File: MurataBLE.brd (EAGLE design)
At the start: 50 x 50 mm, 33 parts, among them IC1 IC_LDO_XX1117, IC3 74LVC1G04DCK, Q2 12MHz, SW1 SW_TACTSW_2PP8073, SW2 SW_TACTSW_2PP8073, SW3 SW_TACTSW_2PP8073, U1 IC_BLE_LBCA2HNZYZ-711, X1 TSW-112-02-S-S

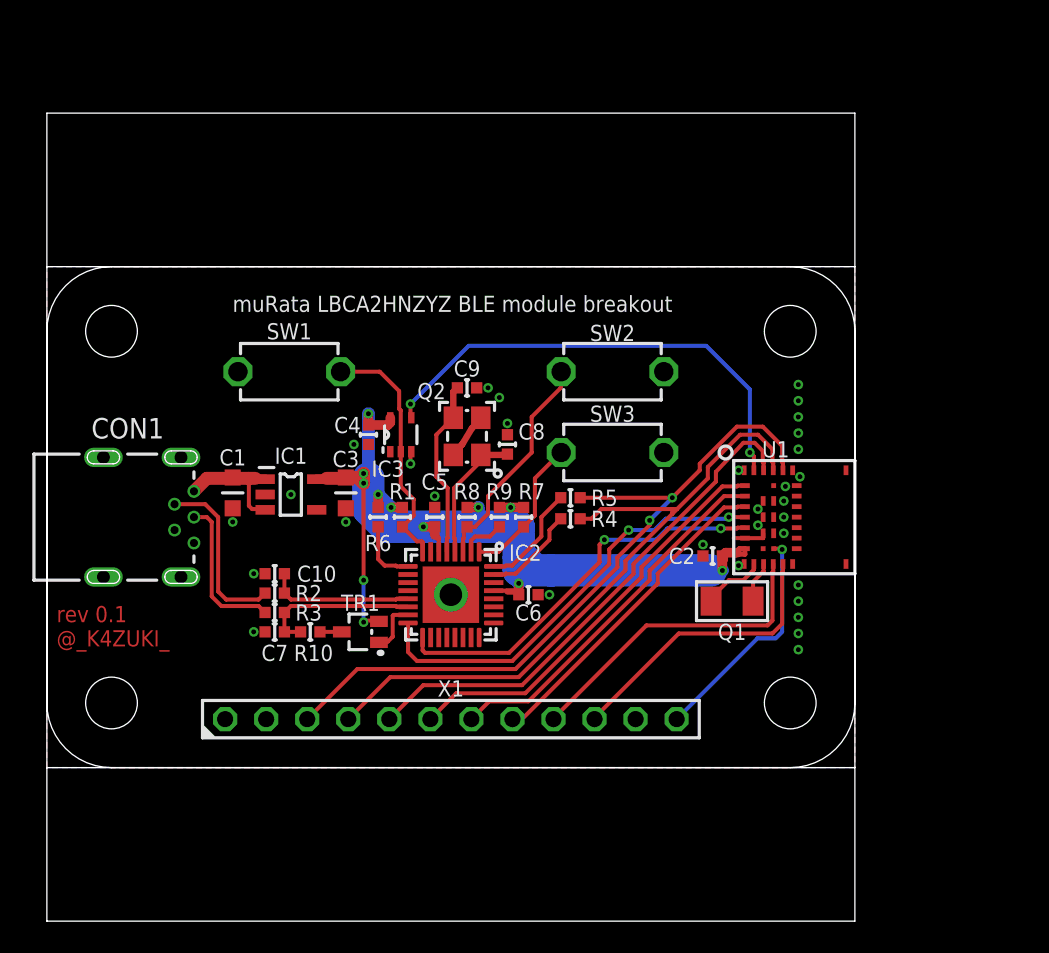
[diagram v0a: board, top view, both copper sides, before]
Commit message: [ BRD ] removed panel frame
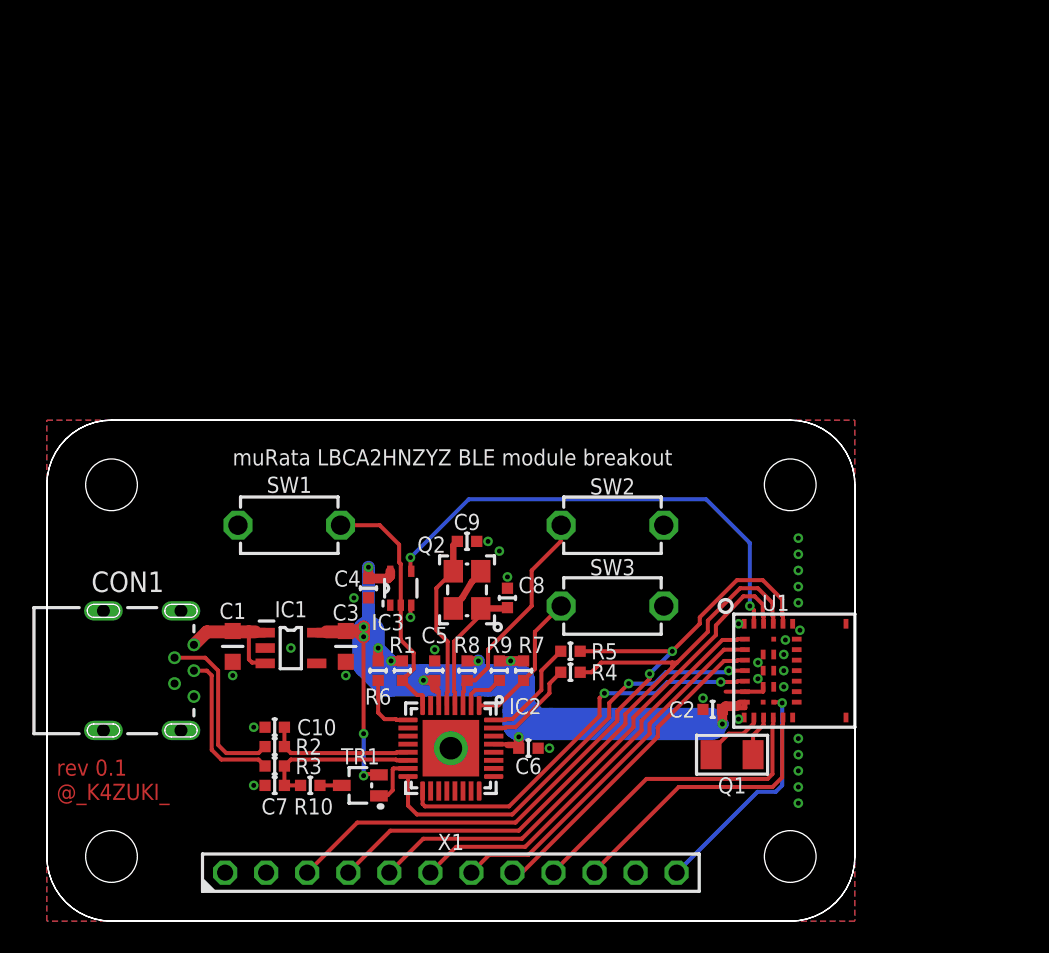
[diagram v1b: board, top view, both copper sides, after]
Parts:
- moved C2 9.50 mm to (41.2, 13.1)
- moved R3 9.50 mm to (14.1, 9.60)
- moved C1 9.50 mm to (11.5, 17.0)
- moved C10 9.50 mm to (14.1, 12.0)
- moved C3 9.50 mm to (18.5, 17.0)
- moved C4 9.50 mm to (19.9, 20.6)
- moved C5 9.50 mm to (24.0, 15.5)
- moved C6 9.50 mm to (29.8, 10.7)
- moved C8 9.50 mm to (28.5, 20.0)
- moved C9 9.50 mm to (26.0, 23.5)
- moved CON1 9.50 mm to (9.10, 15.5)
- moved IC1 9.50 mm to (15.1, 16.9)
- moved IC2 9.50 mm to (25.0, 10.7)
- moved IC3 9.50 mm to (21.9, 20.6)
- moved PCB1 9.50 mm to (25.0, 15.5)
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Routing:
- net GND: track 5.85 -> 6.35 mm
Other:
- board size 50 x 50 mm -> 50 x 31 mm

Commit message: update silk
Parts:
- moved IC3 0.10 mm to (22.0, 20.6)
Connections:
- net 3.3V: now also C3.1; no longer C3.P$1
- net GND: now also C1.2, C3.2; no longer C1.P$2, C3.P$2
- net VUSB: now also C1.1; no longer C1.P$1
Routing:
- net 3.3V: track 72.9 -> 72.1 mm
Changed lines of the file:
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@@
 <wire x1="19" y1="15.5" x2="19" y2="16.6" width="0.15" layer="41"/>
 <wire x1="19" y1="16.6" x2="19" y2="17.3" width="0.15" layer="41"/>
-<wire x1="22.3" y1="19.2" x2="22.3" y2="19.9" width="0.15" layer="41"/>
-<wire x1="22.8" y1="19.2" x2="22.8" y2="19.9" width="0.15" layer="41"/>
-<wire x1="22.8" y1="19.9" x2="22.3" y2="19.9" width="0.15" layer="41"/>
+<wire x1="22.4" y1="19.3" x2="22.4" y2="19.9" width="0.15" layer="41"/>
+<wire x1="22.9" y1="19.3" x2="22.9" y2="19.9" width="0.15" layer="41"/>
+<wire x1="22.9" y1="19.9" x2="22.4" y2="19.9" width="0.15" layer="41"/>
 <wire x1="20.3" y1="19.6" x2="20.3" y2="20.4" width="0.15" layer="41"/>
 <wire x1="20.3" y1="20.4" x2="19.5" y2="20.4" width="0.15" layer="41"/>
@@
 <attribute name="VALUE" x="13.5" y="7.7" size="1" layer="27" font="vector" ratio="20"/>
 </element>
-<element name="IC3" library="74xx-little-us_local" package="SC70-5" value="74LVC1G04DCK" x="21.9" y="20.6" smashed="yes">
-<attribute name="NAME" x="21.1" y="18.5" size="1" layer="25" font="vector" ratio="20" align="center"/>
-<attribute name="VALUE" x="19.4" y="18.1" size="1" layer="27" font="vector" ratio="20"/>
+<element name="IC3" library="74xx-little-us_local" package="SC70-5" value="74LVC1G04DCK" x="22" y="20.6" smashed="yes">
+<attribute name="NAME" x="21" y="23" size="1" layer="25" font="vector" ratio="20" align="center"/>
+<attribute name="VALUE" x="19.5" y="18.1" size="1" layer="27" font="vector" ratio="20"/>
 </element>
 <element name="SW2" library="mylib" package="SW_TACTSW_P8073" value="SW_TACTSW_2PP8073" x="35" y="24.5" smashed="yes" rot="R180">
@@
 <contactref element="IC2" pad="EXP"/>
 <contactref element="CON1" pad="GND"/>
-<contactref element="C3" pad="P$2"/>
-<contactref element="C1" pad="P$2"/>
+<contactref element="C3" pad="2"/>
+<contactref element="C1" pad="2"/>
 <contactref element="IC3" pad="3"/>
 <contactref element="IC3" pad="3"/>
@@
 <via x="18.5" y="15.2" extent="1-16" drill="0.3" diameter="0.45"/>
 <via x="19" y="20" extent="1-16" drill="0.3" diameter="0.45"/>
-<via x="22.5" y="18.8" extent="1-16" drill="0.3" diameter="0.45"/>
+<via x="22.6" y="18.8" extent="1-16" drill="0.3" diameter="0.45"/>
 <via x="28" y="22.9" extent="1-16" drill="0.3" diameter="0.45"/>
 <via x="27.3" y="23.5" extent="1-16" drill="0.3" diameter="0.45"/>
@@
 <wire x1="43.2" y1="14.2" x2="44.325" y2="14.2" width="0.25" layer="1"/>
 <wire x1="44.325" y1="14.2" x2="44.325" y2="14.5" width="0.25" layer="1"/>
-<wire x1="22.55" y1="19.55" x2="22.5" y2="19.55" width="0.25" layer="1"/>
-<wire x1="22.5" y1="19.55" x2="22.5" y2="18.8" width="0.25" layer="1"/>
+<wire x1="22.65" y1="19.65" x2="22.6" y2="19.65" width="0.25" layer="1"/>
+<wire x1="22.6" y1="19.65" x2="22.6" y2="18.8" width="0.25" layer="1"/>
 <contactref element="X1" pad="11"/>
 <contactref element="C10" pad="2"/>
@@
 <contactref element="U1" pad="7"/>
 <contactref element="C2" pad="1"/>
-<contactref element="C3" pad="P$1"/>
+<contactref element="C3" pad="1"/>
 <contactref element="IC2" pad="6"/>
 <contactref element="IC2" pad="29"/>
@@
 <via x="23.3" y="14.9" extent="1-16" drill="0.3"/>
 <via x="26.7" y="16.1" extent="1-16" drill="0.3"/>
-<via x="19.6" y="18.2" extent="1-16" drill="0.3"/>
-<via x="19.6" y="17.6" extent="1-16" drill="0.3"/>
-<wire x1="18.5" y1="17.9525" x2="18.4525" y2="17.9525" width="0.8" layer="1"/>
-<wire x1="18.4525" y1="17.9525" x2="18.4" y2="17.9" width="0.8" layer="1"/>
+<via x="19.9" y="18.2" extent="1-16" drill="0.3"/>
+<via x="19.9" y="17.6" extent="1-16" drill="0.3"/>
 <wire x1="16.7" y1="17.85" x2="17.25" y2="17.85" width="0.6" layer="1"/>
 <wire x1="17.25" y1="17.85" x2="17.3" y2="17.9" width="0.6" layer="1"/>
-<wire x1="18.4" y1="17.9" x2="17.3" y2="17.9" width="0.8" layer="1"/>
-<wire x1="19.6" y1="18.2" x2="19.6" y2="17.6" width="0.8" layer="16"/>
-<wire x1="19.6" y1="18.2" x2="19.3" y2="17.9" width="0.8" layer="1"/>
-<wire x1="19.3" y1="17.9" x2="19.6" y2="17.6" width="0.8" layer="1"/>
-<wire x1="19.6" y1="17.6" x2="19.6" y2="18.2" width="0.8" layer="1"/>
-<wire x1="19.6" y1="18.2" x2="19.9" y2="17.9" width="0.8" layer="16"/>
-<wire x1="19.9" y1="17.9" x2="19.6" y2="17.6" width="0.8" layer="16"/>
-<wire x1="18.5" y1="17.9525" x2="19.2475" y2="17.9525" width="0.8" layer="1"/>
-<wire x1="19.2475" y1="17.9525" x2="19.6" y2="17.6" width="0.8" layer="1"/>
+<wire x1="19.9" y1="18.2" x2="19.6" y2="17.9" width="0.8" layer="1"/>
+<wire x1="19.6" y1="17.9" x2="19.9" y2="17.6" width="0.8" layer="1"/>
+<wire x1="19.9" y1="17.6" x2="19.9" y2="18.2" width="0.8" layer="1"/>
 <wire x1="29.5" y1="16.1" x2="28.7" y2="16.1" width="0.6" layer="1"/>
 <wire x1="28.7" y1="16.1" x2="28" y2="16.1" width="0.6" layer="1"/>
 <wire x1="24" y1="14.9" x2="23.3" y2="14.9" width="0.6" layer="1"/>
 <wire x1="22" y1="16.1" x2="21.3" y2="16.1" width="0.6" layer="1"/>
-<wire x1="20.5" y1="16.9" x2="19.9" y2="17.9" width="0.8" layer="16"/>
 <wire x1="21.3" y1="16.1" x2="21.3" y2="14.9" width="0.8" layer="16"/>
-<wire x1="19.9" y1="17.9" x2="19.9" y2="16" width="2" layer="16"/>
+<wire x1="19.9" y1="17.9" x2="19.9" y2="17.6" width="2" layer="16"/>
+<wire x1="19.9" y1="17.6" x2="19.9" y2="16" width="2" layer="16"/>
 <wire x1="19.9" y1="16" x2="21" y2="14.9" width="2" layer="16"/>
 <wire x1="21" y1="14.9" x2="21.3" y2="14.9" width="2" layer="16"/>
-<wire x1="21.3" y1="14.9" x2="23.3" y2="14.9" width="2" layer="16"/>
+<wire x1="21.3" y1="14.9" x2="22.5" y2="14.9" width="2" layer="16"/>
+<wire x1="22.5" y1="14.9" x2="23.3" y2="14.9" width="2" layer="16"/>
 <wire x1="23.3" y1="14.9" x2="26.7" y2="14.9" width="2" layer="16"/>
 <wire x1="26.7" y1="16.1" x2="26.7" y2="14.9" width="0.8" layer="16"/>
 <via x="19.9" y="21.9" extent="1-16" drill="0.3"/>
 <wire x1="19.9" y1="21.9" x2="19.9" y2="21.2" width="0.6" layer="1"/>
-<wire x1="19.9" y1="21.2" x2="21.1" y2="21.2" width="0.6" layer="1"/>
-<wire x1="21.25" y1="21.65" x2="21.25" y2="21.35" width="0.6" layer="1"/>
-<wire x1="21.25" y1="21.35" x2="21.1" y2="21.2" width="0.6" layer="1"/>
+<wire x1="19.9" y1="21.2" x2="21.2" y2="21.2" width="0.6" layer="1"/>
+<wire x1="21.35" y1="21.55" x2="21.35" y2="21.35" width="0.6" layer="1"/>
+<wire x1="21.35" y1="21.35" x2="21.2" y2="21.2" width="0.6" layer="1"/>
 <wire x1="20.5" y1="16.9" x2="21.3" y2="16.1" width="0.8" layer="16"/>
 <wire x1="26.7" y1="14.9" x2="27.3" y2="14.9" width="2" layer="16"/>
@@
 <via x="29.2" y="11.4" extent="1-16" drill="0.3"/>
 <wire x1="29.2" y1="11.4" x2="29.2" y2="12.2" width="0.8" layer="16"/>
-<wire x1="19.9" y1="21.9" x2="19.9" y2="18.5" width="0.8" layer="16"/>
-<wire x1="19.9" y1="18.5" x2="19.6" y2="18.2" width="0.8" layer="16"/>
 <wire x1="24.25" y1="13.35" x2="24.25" y2="14.15" width="0.25" layer="1"/>
 <wire x1="24.25" y1="14.15" x2="24.2" y2="14.2" width="0.25" layer="1"/>
@@
 <wire x1="19.6" y1="9" x2="19.6" y2="11.6" width="0.25" layer="16"/>
 <via x="19.6" y="11.6" extent="1-16" drill="0.3"/>
-<wire x1="19.6" y1="11.6" x2="19.6" y2="17.6" width="0.25" layer="1"/>
+<wire x1="19.6" y1="11.6" x2="19.6" y2="16.6" width="0.25" layer="1"/>
+<wire x1="19.6" y1="16.6" x2="19.9" y2="16.9" width="0.25" layer="1"/>
+<wire x1="19.9" y1="16.9" x2="19.9" y2="17.6" width="0.25" layer="1"/>
+<wire x1="21.3" y1="16.1" x2="22.5" y2="14.9" width="0.8" layer="16"/>
+<wire x1="19.6" y1="17.9" x2="18.5" y2="17.9" width="0.8" layer="1"/>
+<wire x1="18.5" y1="17.9" x2="17.3" y2="17.9" width="0.8" layer="1"/>
+<wire x1="19.9" y1="21.9" x2="19.9" y2="18.2" width="0.8" layer="16"/>
+<wire x1="19.9" y1="18.2" x2="19.9" y2="17.9" width="0.8" layer="16"/>
 </signal>
 <signal name="RESET">
@@
 <via x="43.5" y="19.5" extent="1-16" drill="0.3"/>
 <via x="22.5" y="22.5" extent="1-16" drill="0.3"/>
-<wire x1="22.55" y1="21.65" x2="22.5" y2="21.7" width="0.25" layer="1"/>
+<wire x1="22.65" y1="21.55" x2="22.5" y2="21.7" width="0.25" layer="1"/>
 <wire x1="22.5" y1="22.5" x2="26.1" y2="26.1" width="0.25" layer="16"/>
 <wire x1="26.1" y1="26.1" x2="40.8" y2="26.1" width="0.25" layer="16"/>
@@
 </signal>
 <signal name="VUSB">
-<contactref element="C1" pad="P$1"/>
+<contactref element="C1" pad="1"/>
 <contactref element="CON1" pad="VBUS"/>
 <contactref element="IC1" pad="1"/>
 <contactref element="IC1" pad="3"/>
 <wire x1="9.1" y1="17.1" x2="9.9" y2="17.9" width="0.8" layer="1"/>
-<wire x1="11.5" y1="17.9525" x2="11.5" y2="17.9" width="0.8" layer="1"/>
 <wire x1="11.5" y1="17.9" x2="9.9" y2="17.9" width="0.8" layer="1"/>
 <wire x1="13.51" y1="17.85" x2="12.95" y2="17.85" width="0.6" layer="1"/>
@@
 <wire x1="22" y1="14.9" x2="22.7" y2="15.6" width="0.25" layer="1"/>
 <wire x1="22.7" y1="15.6" x2="22.7" y2="16.6" width="0.25" layer="1"/>
-<wire x1="22.7" y1="16.6" x2="21.9" y2="17.4" width="0.25" layer="1"/>
-<wire x1="21.9" y1="17.4" x2="21.9" y2="19.55" width="0.25" layer="1"/>
-<wire x1="21.9" y1="19.55" x2="21.9" y2="22.1" width="0.25" layer="1"/>
-<wire x1="21.9" y1="22.1" x2="21.8" y2="22.2" width="0.25" layer="1"/>
+<wire x1="22.7" y1="16.6" x2="22" y2="17.3" width="0.25" layer="1"/>
+<wire x1="22" y1="17.3" x2="22" y2="19.65" width="0.25" layer="1"/>
+<wire x1="22" y1="19.65" x2="22" y2="22" width="0.25" layer="1"/>
+<wire x1="22" y1="22" x2="21.8" y2="22.2" width="0.25" layer="1"/>
 <wire x1="21.8" y1="23.3" x2="21.8" y2="22.2" width="0.25" layer="1"/>
 <wire x1="18.175" y1="24.5" x2="20.6" y2="24.5" width="0.25" layer="1"/>

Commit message: [ FIX ] library update
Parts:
- moved C4 1.65 mm to (20.3, 22.2), turned to 90 degrees
- moved R8 0.86 mm to (26.5, 16.2), turned to 90 degrees
- moved R6 0.76 mm to (20.8, 16.2), turned to 90 degrees
- moved R7 0.73 mm to (29.3, 16.2), turned to 90 degrees
- moved R9 0.71 mm to (27.9, 16.2), turned to 90 degrees
- moved R1 0.70 mm to (22.0, 16.2), turned to 90 degrees
- moved IC3 0.40 mm to (22.4, 20.6)
- moved C8 0.32 mm to (28.4, 20.3)
- moved C9 0.32 mm to (25.9, 23.8)
- moved Q2 0.32 mm to (25.9, 20.8)
- moved C3 0.30 mm to (18.2, 17.0)
- moved C1 0.20 mm to (11.3, 17.0)
- moved IC1 0.20 mm to (14.9, 16.9)
- moved C5 0.10 mm to (24.1, 15.5)
- moved Q1 0.10 mm to (42.3, 10.3)
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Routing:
- net 3.3V: track 72.1 -> 60.9 mm, vias 12 -> 13
- net GND: track 6.45 -> 14.0 mm, vias 33 -> 41
- net N$4: track 4.04 -> 6.27 mm
- net N$5: track 2.80 -> 4.37 mm
- net RESET: track 29.7 -> 29.0 mm

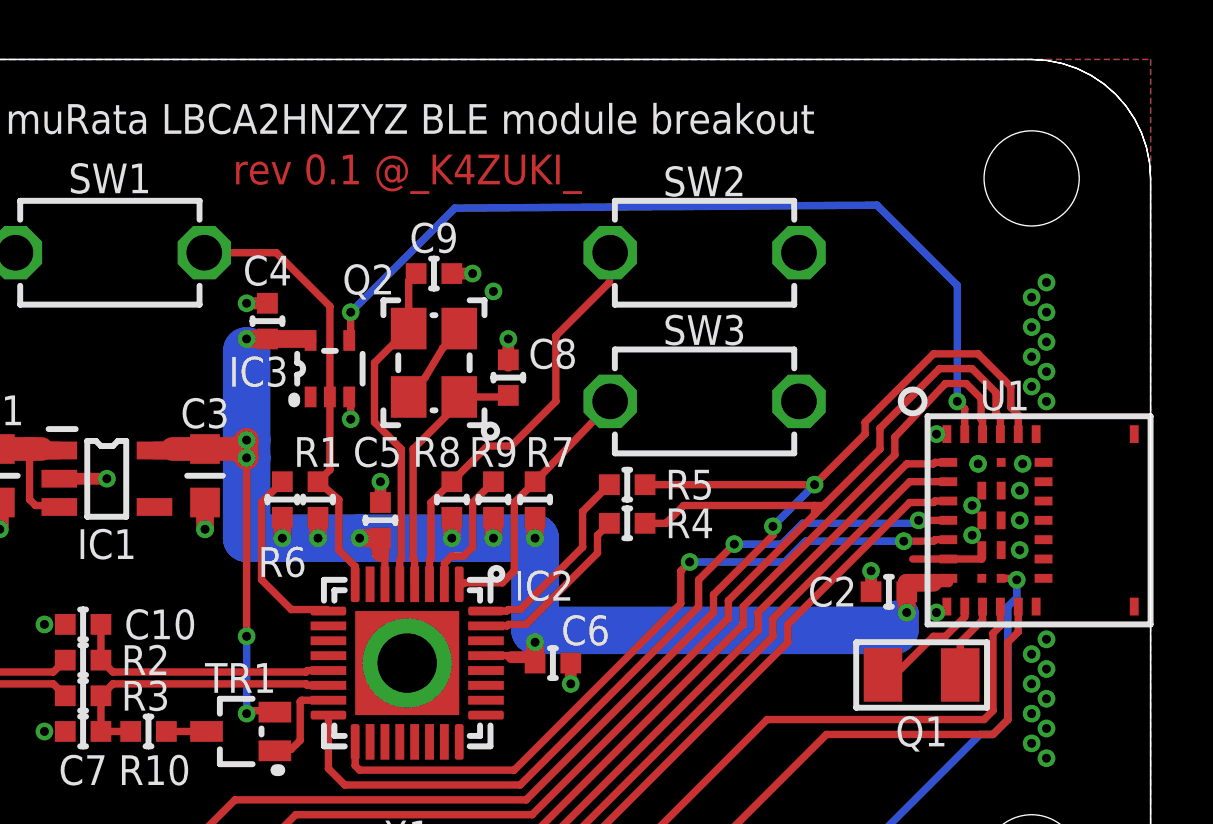
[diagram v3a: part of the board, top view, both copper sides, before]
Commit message: [ FIX ] MurataBLE
small schema change
library update
increase GND via
C2 moved
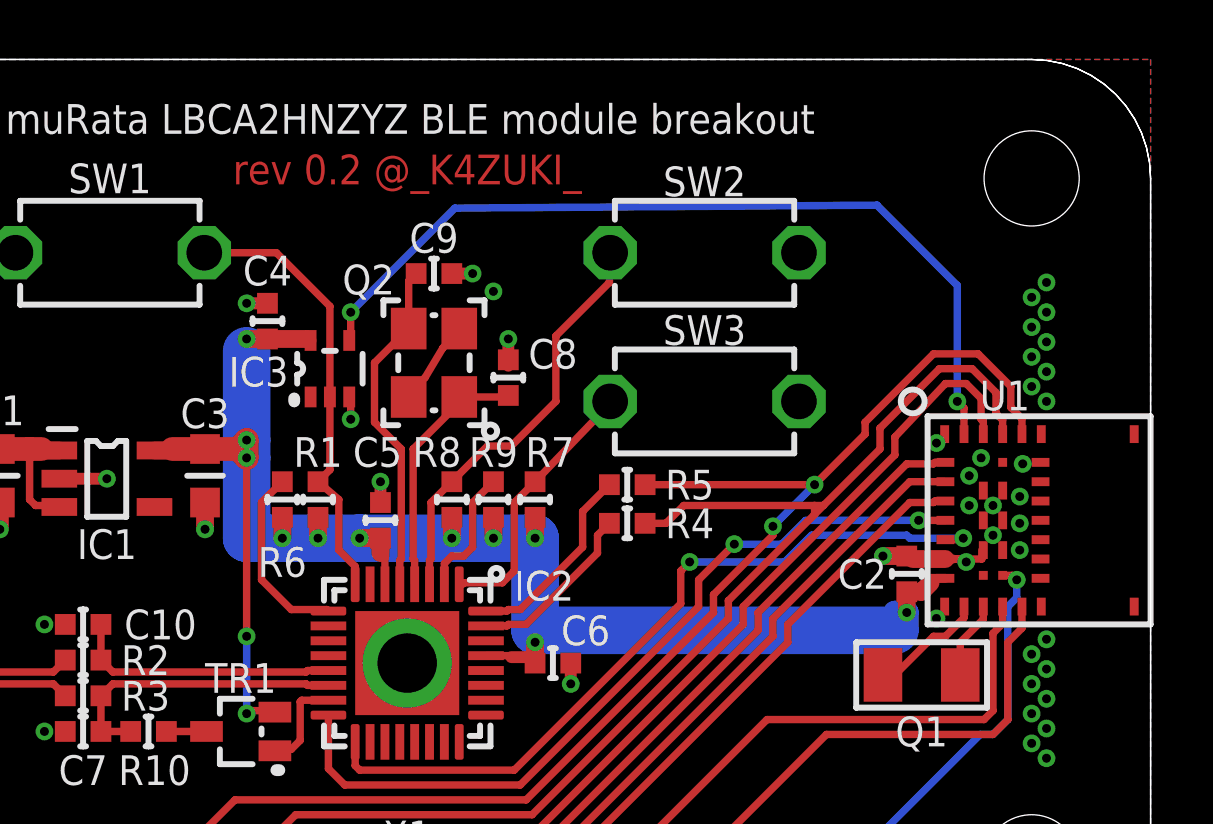
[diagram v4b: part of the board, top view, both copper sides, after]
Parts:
- moved C2 0.85 mm to (41.8, 13.7), turned to 90 degrees
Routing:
- net SWDIO: track 24.7 -> 25.9 mm
- net 3.3V: track 60.9 -> 60.0 mm
- net GND: track 14.0 -> 14.9 mm, vias 41 -> 44
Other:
- board text added: "rev 0.2 @_K4ZUKI_"
- board text removed: "rev 0.1 @_K4ZUKI_"

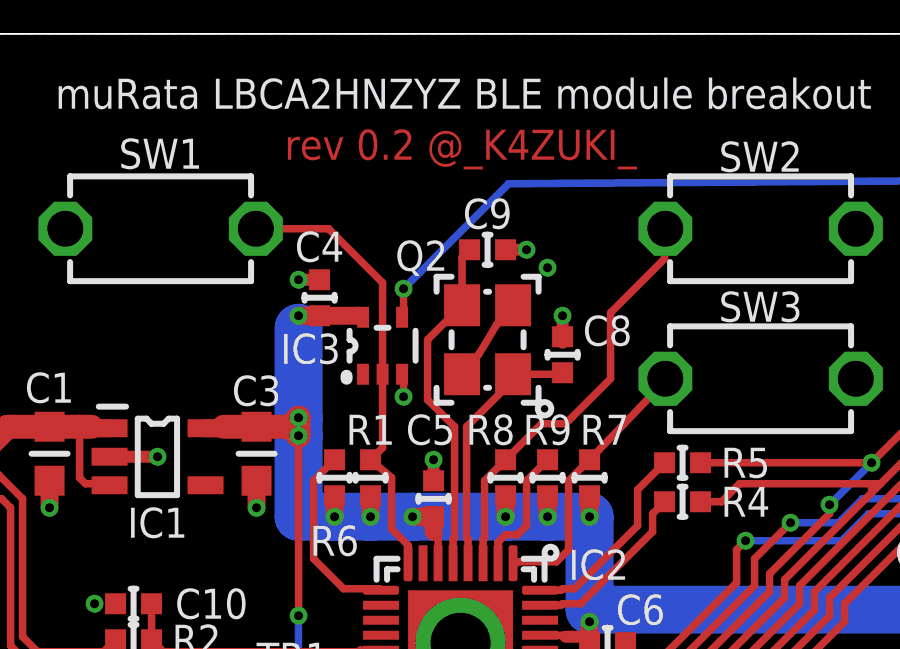
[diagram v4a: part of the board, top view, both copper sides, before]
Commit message: [ FIX ] fix trace, increase via
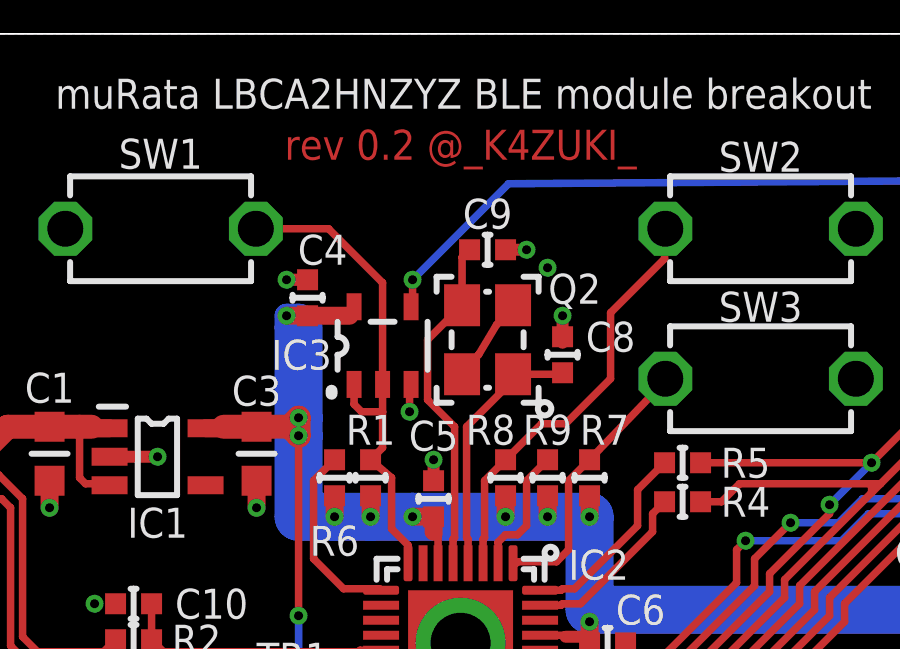
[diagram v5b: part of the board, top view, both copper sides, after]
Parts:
- IC3: value 74LVC1G04DCK -> 74LVC1G00DBV; device 74xx-little-us_local:SC70-5 -> 74xx-little-us_local:SOT23-5
- moved C4 0.40 mm to (19.9, 22.2)
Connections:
- net !RESET!: now also IC3.1
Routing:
- net !RESET!: track 15.0 -> 16.7 mm
- net 3.3V: track 60.0 -> 61.6 mm
